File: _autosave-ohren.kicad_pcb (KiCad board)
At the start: 2 copper layers, 60 x 28.7 mm, 74 parts, among them J1 Conn_01x19_Male, U1 TLC5951RHA

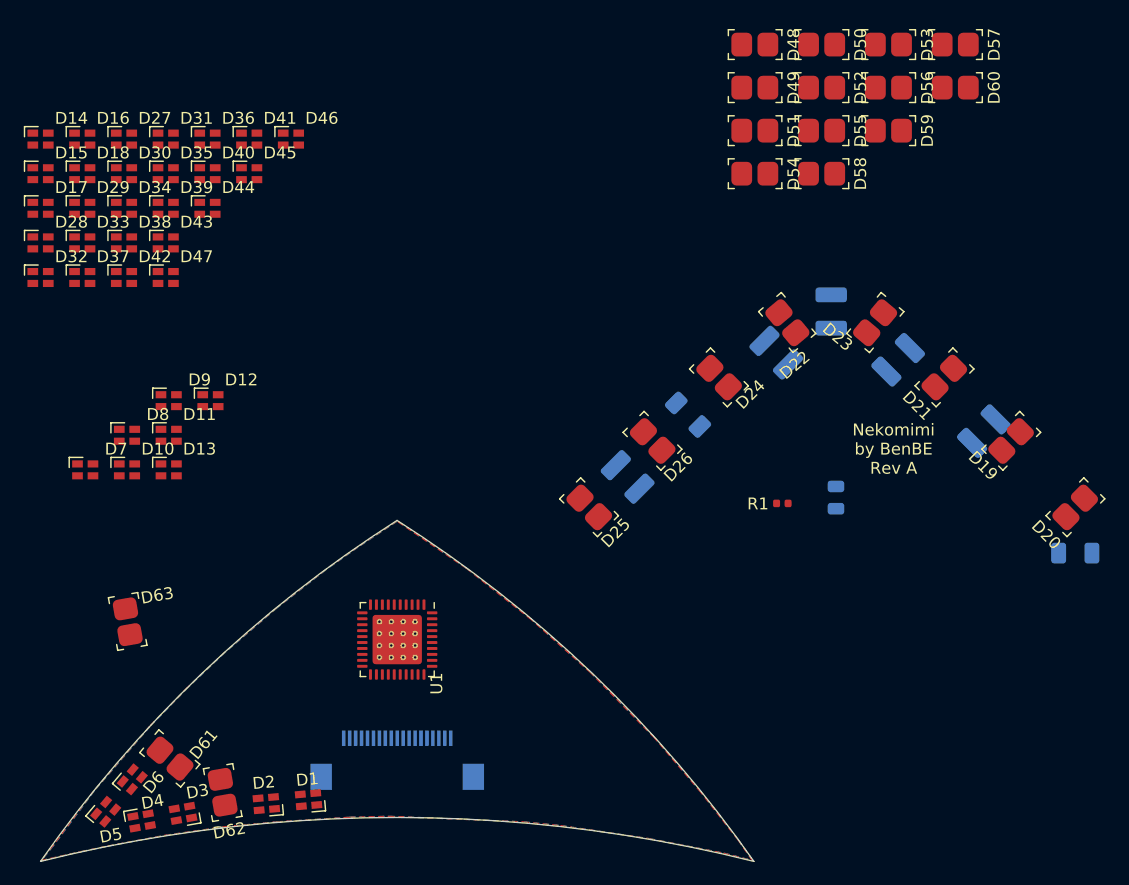
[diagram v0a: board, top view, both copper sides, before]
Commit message: Switch to LEDs with integrated controller
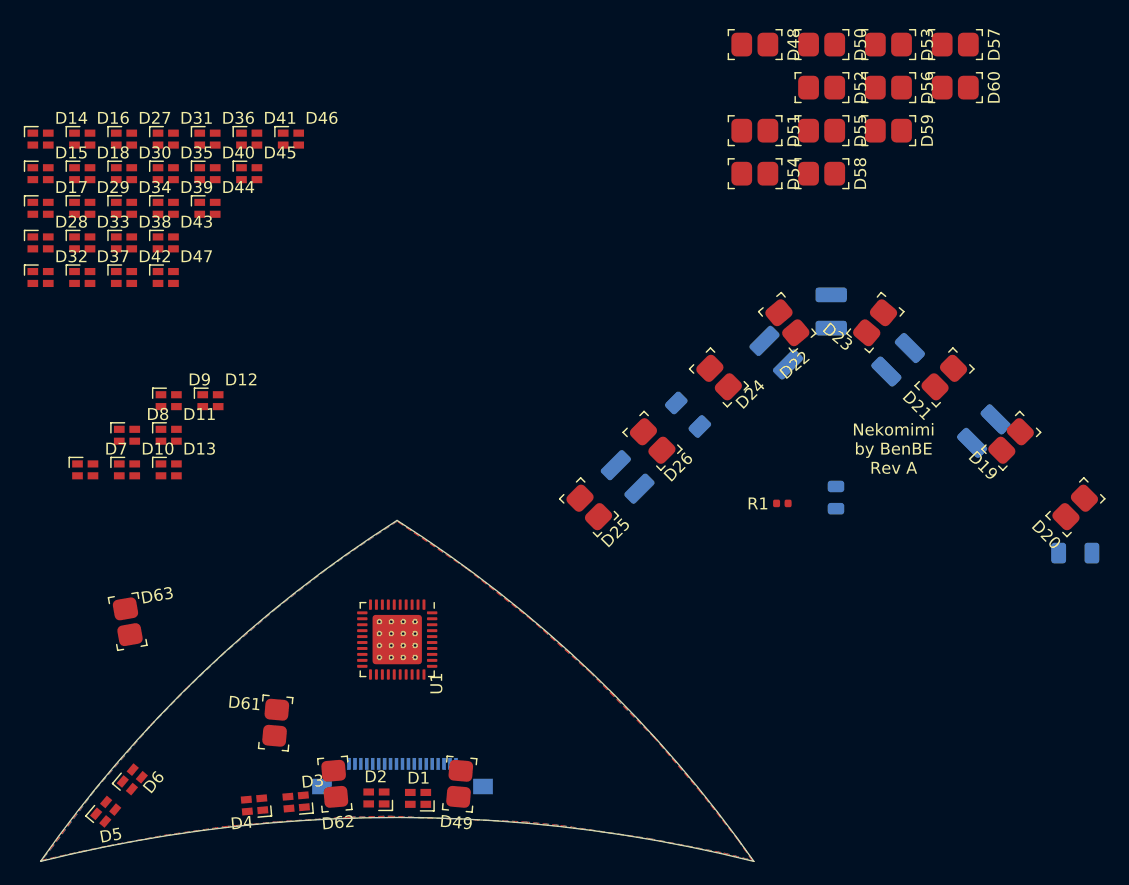
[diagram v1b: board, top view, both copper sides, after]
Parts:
- J1: footprint Connector_FFC-FPC:Hirose_FH12-19S-0.5SH_1x19-1MP_P0.50mm_Horizontal -> catear-pcb:Molex_Easy-On_54550-1971_1x19_P0.5mm_Horizontal
- moved D49 63.6 mm to (145.2, 109.5), turned to 265 degrees
- moved D4 9.60 mm to (128.0, 111.2), turned to 185 degrees
- moved D3 9.57 mm to (131.5, 111.0), turned to 185 degrees
- moved D62 9.46 mm to (134.8, 109.5), turned to 275 degrees
- moved D61 9.39 mm to (129.8, 104.4), turned to 265 degrees
- moved D2 9.27 mm to (138.2, 110.7), turned to 180 degrees
- moved D1 9.21 mm to (141.8, 110.7), turned to 180 degrees
- moved J1 0.92 mm to (140.4, 108.3)
